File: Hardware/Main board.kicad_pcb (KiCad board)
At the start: 4 copper layers, 60.7 x 40 mm, 164 parts, among them IC1 LTC4413EDD#PBF, J1 ST1W008S4TR2000, J2 USB_C_Receptacle_USB2.0, J3 XT30PW-M, J4 USB_C_Receptacle_USB2.0, J5 7788, J6 7788, Q1 SISS23DN-T1-GE3, Q2 BSZ025N04LS, Q3 BSZ025N04LS, Q4 BSZ025N04LS, Q6 SSM3K15AMFV,L3F, U1 ESP32-S3, U10 TPS55288QRPMRQ1, U11 DPS368, U12 TCMT1109, U2 SN65HVD230, U3 LM66200DRLR, U4 MAX77827AEFD+T, U5 SC4215ASTRT, U7 BU27006MUC-ZTR, U8 INA219AxDCN, Y1 R940000171

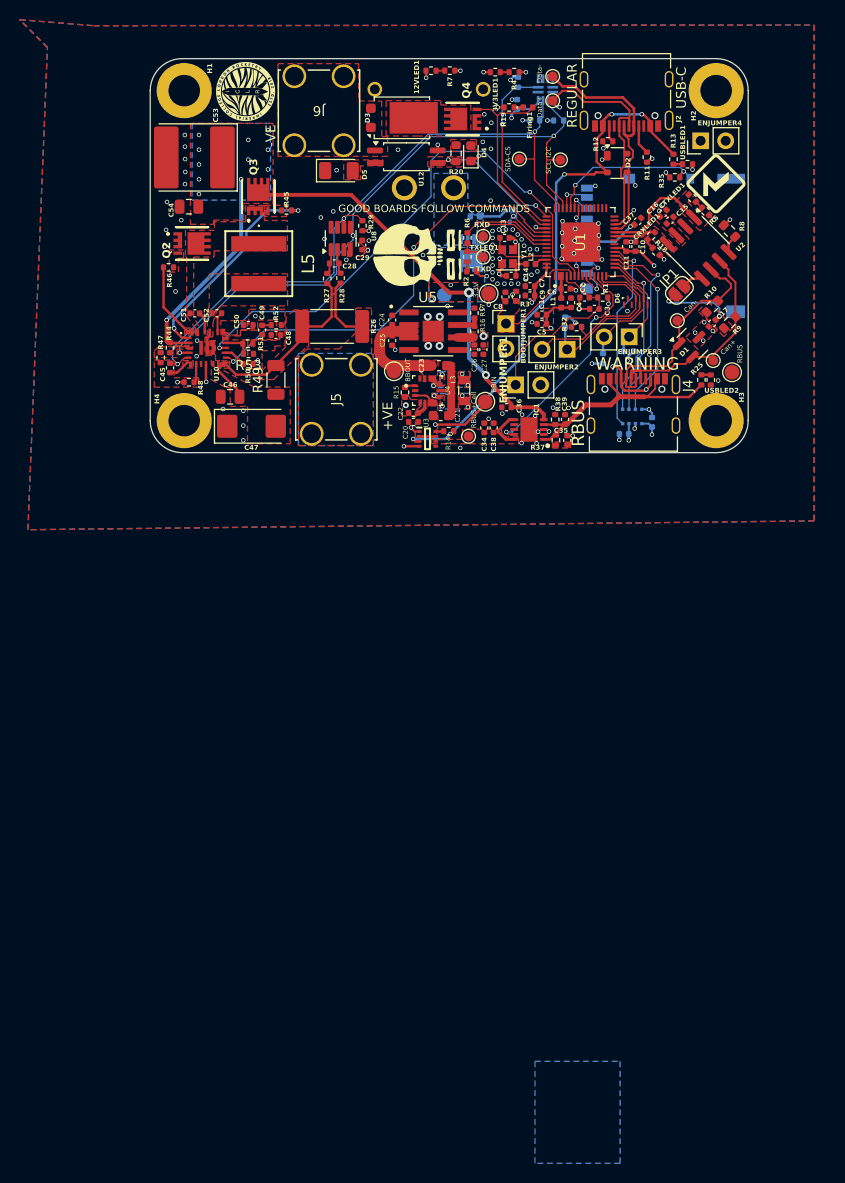
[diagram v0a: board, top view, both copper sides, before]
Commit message: Added voltage ref for post ideal diode
(more firmware too)
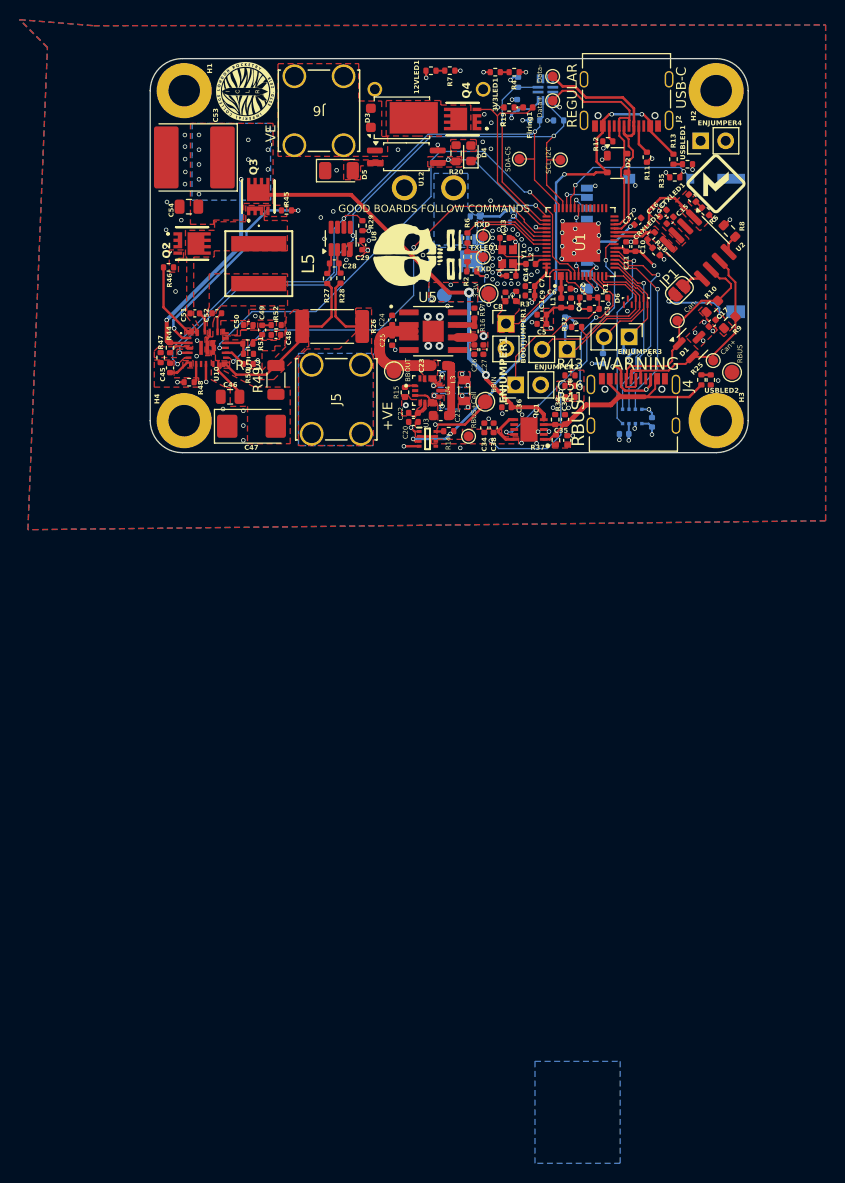
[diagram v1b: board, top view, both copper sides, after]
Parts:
- added C56: 0.1uF, Capacitor_SMD:C_0402_1005Metric, F.Cu at (127.6, 105.7)
- added R41: 1.5k, Resistor_SMD:R_0402_1005Metric, F.Cu at (127.6, 104.5)
- added R43: 470, Resistor_SMD:R_0402_1005Metric, F.Cu at (127.6, 103.5)
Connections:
- U1 pad 21: unconnected-(U1-GPIO15/ADC2_CH4/XTAL_32K_P-Pad21) -> /BatteryV_LOG
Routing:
- net /BatteryV_LOG: track 0.00 -> 16.8 mm, vias 0 -> 2
- net /Power/RBUS + Cell: track 4.13 -> 16.6 mm, vias 0 -> 2
- net GND: vias 124 -> 123
- added copper zone on F.Cu, net /BatteryV_LOG

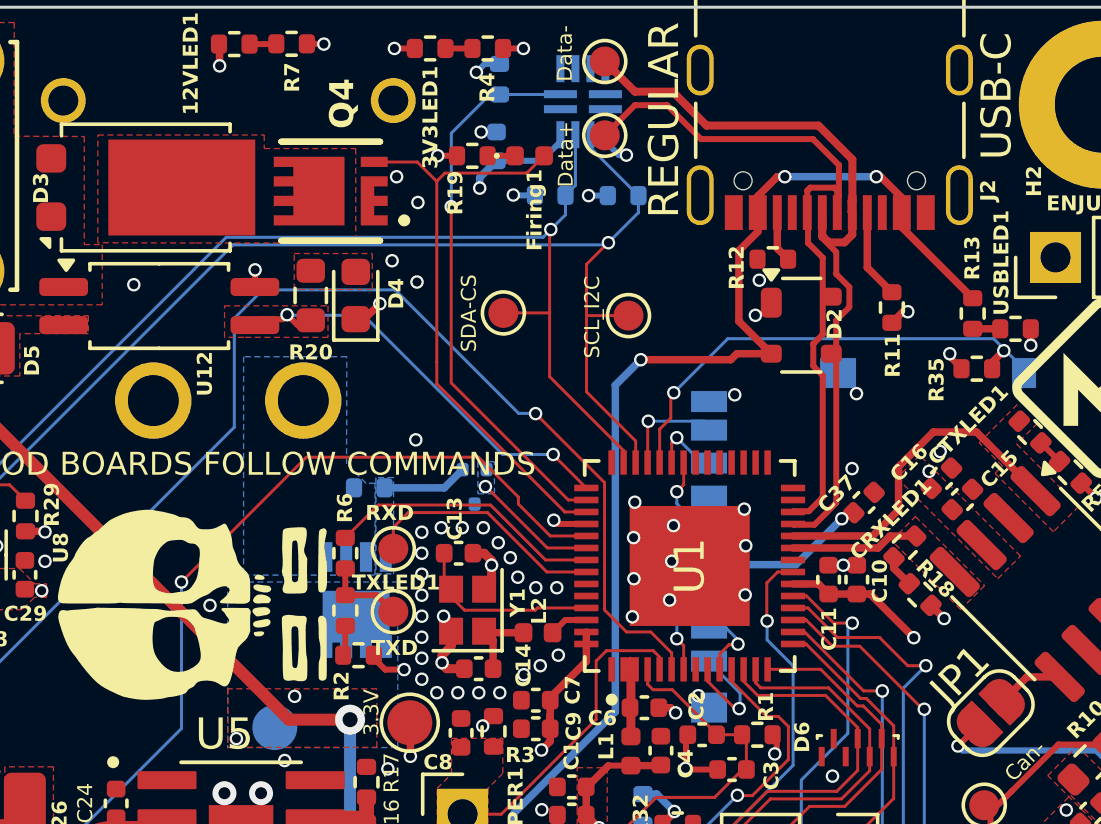
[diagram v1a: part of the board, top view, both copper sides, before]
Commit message: Moved a 3V3 decoupling capacitor for ESP32
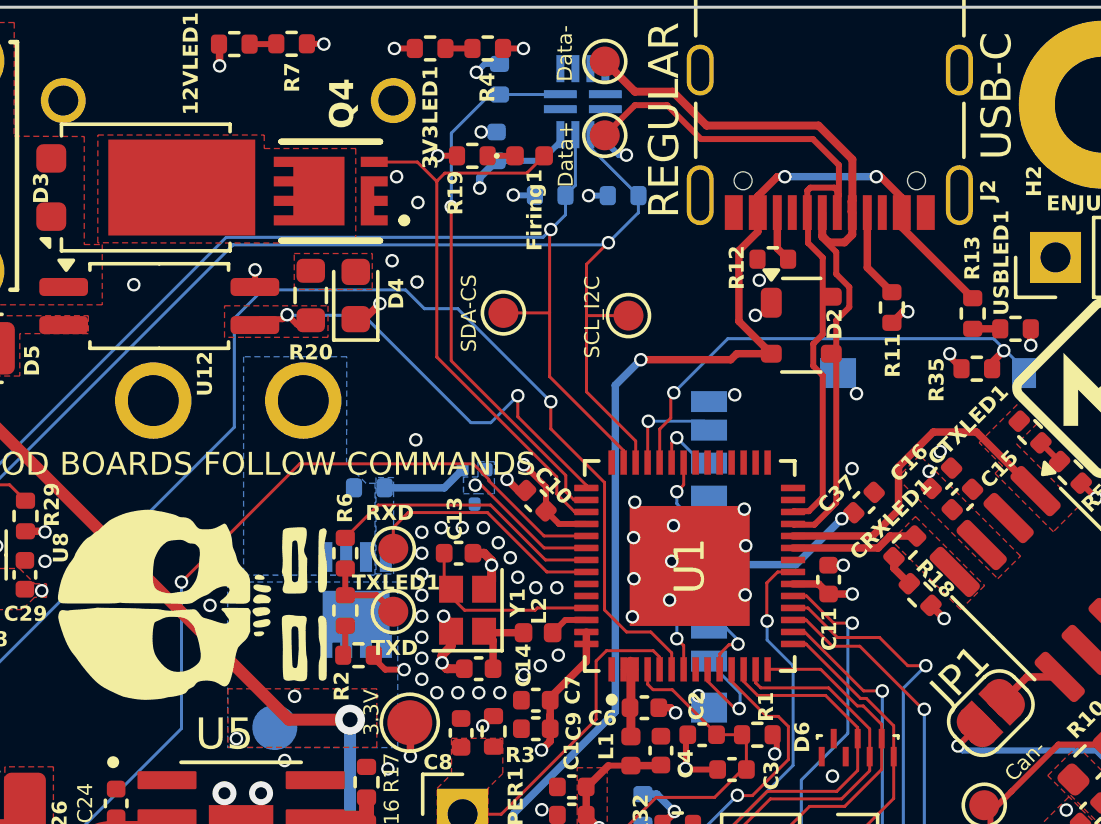
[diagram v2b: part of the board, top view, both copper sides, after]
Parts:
- moved C10 11.0 mm to (123.5, 87.8), turned to 135 degrees
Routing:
- net /Cont 1: track 14.7 -> 15.9 mm
- net GND: track 46.7 -> 46.1 mm, vias 123 -> 124
- net /Current_sens: track 55.3 -> 55.8 mm

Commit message: Mega commit
Post review changes
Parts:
- removed 12VLED1: RED_LED, Resistor_SMD:R_0402_1005Metric
- removed R26: 2m, Resistor_SMD:R_2512_6332Metric_Pad1.40x3.35mm_HandSolder
- removed R29: 3.3k, Resistor_SMD:R_0402_1005Metric
- removed R43: 470, Resistor_SMD:R_0402_1005Metric
- added C57: 0.1uF, Capacitor_SMD:C_0402_1005Metric, F.Cu at (136.3, 99.0)
- added LED5: RED_LED, LED_SMD:LED_0402_1005Metric, F.Cu at (101.0, 100.0)
- added R23: 10k, Resistor_SMD:R_0402_1005Metric, F.Cu at (136.3, 99.9)
- added R24: 1.8k, Resistor_SMD:R_0402_1005Metric, F.Cu at (136.3, 100.9)
- added R39: 10k, Resistor_SMD:R_0402_1005Metric, F.Cu at (119.7, 76.1)
- added R40: 10k, Resistor_SMD:R_0402_1005Metric, F.Cu at (127.5, 104.6)
- 3V3LED1, CRXLED1, CTXLED1, TXLED1, USBLED1: footprint Resistor_SMD:R_0402_1005Metric -> LED_SMD:LED_0402_1005Metric
- C37: moved to B.Cu
- R37: value 1 -> 1R
- R41: value 1.5k -> 18k
- R48: value 50k -> 49.9k
- R51, R53: value 165k -> 110k
- RBUSLED1: renamed from USBLED2; footprint Resistor_SMD:R_0402_1005Metric -> LED_SMD:LED_0402_1005Metric
- moved R7 31.4 mm to (100.0, 100.0), turned to 90 degrees
- moved C37 7.33 mm to (127.4, 89.7), turned to -90 degrees
- moved R27 6.22 mm to (103.3, 99.9)
- moved C28 6.22 mm to (104.0, 98.3)
- moved C29 6.22 mm to (106.9, 96.5)
- moved R28 6.22 mm to (104.7, 99.8)
- moved U8 6.22 mm to (104.7, 95.8)
- moved Q6 5.18 mm to (117.7, 90.9)
- moved Q1 4.95 mm to (112.9, 89.3), turned to 180 degrees
- moved C4 3.22 mm to (124.7, 97.4), turned to 180 degrees
- moved R36 2.94 mm to (116.3, 89.8), turned to 90 degrees
- moved R1 2.84 mm to (128.1, 95.9)
- moved Firing1 2.62 mm to (120.7, 76.1), turned to -90 degrees
- moved D6 2.44 mm to (131.8, 96.1)
- moved TP12 2.32 mm to (124.9, 80.1)
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- renumbered ENJUMPER4 to 3V3_GND1, ENJUMPER2 to GPIO_7/8, ENJUMPER3 to GPIO_9/10
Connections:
- net /Chip_Selec renamed /CS_Baro
- net /INT renamed /BuckBoost_INT
- net /MISO renamed /MISO_Baro
- net /MOSI renamed /MOSI_Baro
- D6 pad 1: unconnected-(D6-K/A_1-Pad1) -> /GPIO7
- D6 pad 3: /GPIO8 -> /GPIO10
- D6 pad 4: /GPIO10 -> unconnected-(D6-K/A_3-Pad4)
- D6 pad 5: unconnected-(D6-K/A_4-Pad5) -> /GPIO8
- D6 pad 6: /GPIO7 -> /GPIO9
- D6 pad 7: /GPIO9 -> unconnected-(D6-K/A_6-Pad7)
- IC1 pad 9: /Stat -> /ID_Stat
- J4 pad A4: RBUS_uC_V -> +16.8V
- J4 pad A5: GND -> RBUS_uC_V
- J4 pad A8: +16.8V -> unconnected-(J4-SBU1-PadA8)
- J4 pad A9: RBUS_uC_V -> +16.8V
- J4 pad B4: RBUS_uC_V -> +16.8V
- J4 pad B5: GND -> RBUS_uC_V
- J4 pad B9: RBUS_uC_V -> +16.8V
- R27 pad 1: /Voltage Regulation/ISN_2 -> /PyroPWR
- R28 pad 1: /PyroPWR -> /Voltage Regulation/VOUT_2
- R41 pad 2: /Power/RBUS + Cell -> GND
- R42 pad 1: /Interrupt  -> /Interrupt_photo
- R49 pad 2: /Voltage Regulation/ISN_2 -> /PyroPWR
- R7 pad 1: +12V -> /PyroPWR
- U1 pad 11: /Stat -> /GPIO7
- U1 pad 12: /GPIO7 -> /GPIO8
- U1 pad 13: /GPIO8 -> /GPIO9
- U1 pad 14: /GPIO9 -> /GPIO10
- U1 pad 15: /GPIO10 -> /DeployV_LOG
- U1 pad 42: unconnected-(U1-GPIO37-Pad42) -> /Interrupt_photo
- U1 pad 43: /Cont 1 -> /Nuke 1
- U1 pad 44: /Interrupt  -> /Cont 1
- U1 pad 45: /Nuke 1 -> /Current_sens
- U1 pad 6: /Current_sens -> /ID_Stat
- U10 pad 13: /Voltage Regulation/ISN_2 -> /PyroPWR
- U10 pad 29: /Voltage Regulation/ISN_2 -> /PyroPWR
- U7 pad 6: /Interrupt  -> /Interrupt_photo
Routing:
- net Cell_+: track 65.1 -> 39.5 mm, vias 16 -> 41
- net /Stat: track 22.9 -> 0.00 mm, vias 2 -> 0
- net /ID_Stat: track 0.00 -> 21.5 mm, vias 0 -> 2
- net /Interrupt : track 18.5 -> 0.00 mm, vias 1 -> 0
- net /Voltage Regulation/ISN_2: track 18.1 -> 0.00 mm
- net +16.8V: track 0.00 -> 17.7 mm, vias 0 -> 2
- net /Interrupt_photo: track 0.00 -> 16.7 mm, vias 0 -> 1
- net /Voltage Regulation/VOUT_2: track 4.22 -> 18.2 mm
- net RBUS_uC_V: track 27.8 -> 14.2 mm
- net /Current_sens: track 55.8 -> 42.3 mm
- net GND: track 46.1 -> 33.7 mm, vias 124 -> 121
- net /PyroPWR: track 6.72 -> 17.8 mm, vias 0 -> 9
- net /DeployV_LOG: track 0.00 -> 7.97 mm
- net /GPIO7: track 18.9 -> 11.3 mm
- net /Cell-switch: track 4.57 -> 10.4 mm
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- added copper zone on F.Cu, net /DeployV_LOG
- added copper zone on F.Cu, net /Nuke 1
- added copper zone on B.Cu, net Net-(D3-A-Pad1)
- added copper zone on B.Cu, net Net-(D3-K)
- added copper zone on F.Cu, net RBUS_uC_V
- removed copper zone on B.Cu, net /Cell-switch
- removed copper zone on F.Cu, net /Voltage Regulation/ISN_2

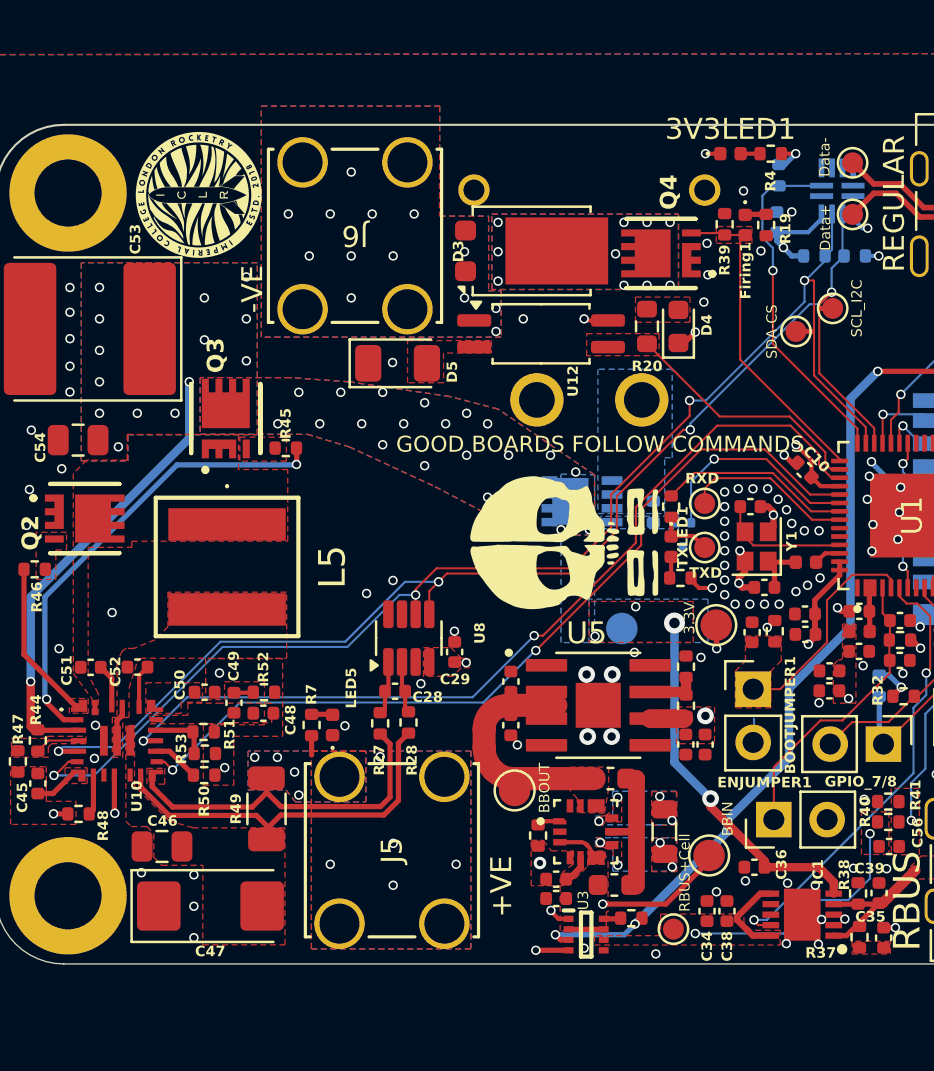
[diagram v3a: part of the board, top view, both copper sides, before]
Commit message: Silkscreen label
Made sure PCB file was saved before push...
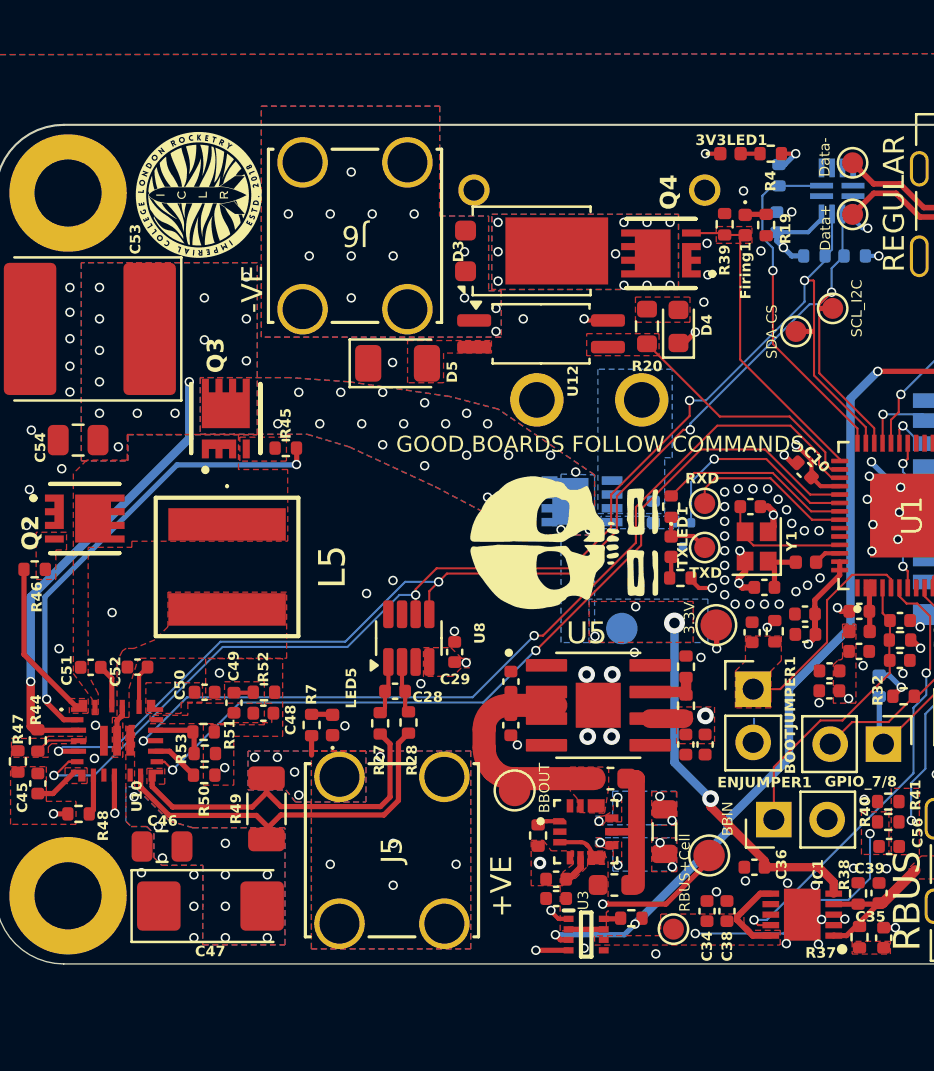
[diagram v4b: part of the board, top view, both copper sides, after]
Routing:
- net /Voltage Regulation/VOUT_2: vias 0 -> 9
- added copper zone on B.Cu, net /Voltage Regulation/VOUT_2
